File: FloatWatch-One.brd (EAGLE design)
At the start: 25.4 x 40 mm, 53 parts, among them Q1 S8050, Q2 S8050, U1 ATMEGA168P-QFN32, U2 ADXL345, U3 MCP6001-SOT23, U4 APDS-9008, U5 TP4055, U6 3.3V, U7 CH340E, Y1 7.3728MHz

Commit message: Rename to FloatWatch
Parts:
- removed POVLOGO: (no value), MyLibrary:ICON-PW
- added U$1: (no value), MyLibrary:ICON-OSHW
- moved CELOGO 2.01 mm to (19.7, 12.1)
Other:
- board text added: "Design by geneLocated"
- board text added: "Devised & Assembled in China"
- board text added: "FloatWatch"
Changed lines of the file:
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@@
 <board>
 <plain>
-<text x="8.8865" y="38.09" size="0.45" layer="22" font="vector" rot="MR180" align="bottom-right">Ver 1.1</text>
+<text x="19.685" y="34.925" size="0.8128" layer="22" font="vector" rot="MR0">Ver 1.1</text>
 <wire x1="1.27" y1="5.08" x2="0" y2="3.81" width="0" layer="20" curve="90"/>
 <wire x1="0" y1="3.81" x2="0" y2="1.27" width="0" layer="20"/>
@@
 <wire x1="1.27" y1="8.255" x2="24.13" y2="8.255" width="0" layer="20"/>
 <wire x1="24.13" y1="5.08" x2="1.27" y2="5.08" width="0" layer="20"/>
+<text x="19.685" y="36.195" size="1.778" layer="22" font="vector" rot="MR0">FloatWatch</text>
+<text x="19.685" y="10.795" size="0.762" layer="22" font="vector" rot="MR0">Design by geneLocated</text>
+<text x="19.685" y="10.16" size="0.5842" layer="22" font="vector" rot="MR0">Devised &amp; Assembled in China</text>
 </plain>
 <attributes>
@@
 </element>
 <element name="TS1" library="MyLibrary" package="TS-3X4P" value="TS-P" x="23.8125" y="24.13" rot="R90"/>
-<element name="CELOGO" library="MyLibrary" package="ICON-CE" value="" x="20.32" y="10.16" rot="MR0"/>
-<element name="POVLOGO" library="MyLibrary" package="ICON-PW" value="" x="18.7325" y="36.195" rot="MR0"/>
+<element name="CELOGO" library="MyLibrary" package="ICON-CE" value="" x="19.685" y="12.065" rot="MR0"/>
 <element name="U5" library="MyLibrary" package="SOT23-5" value="TP4055" x="6.985" y="35.8775" smashed="yes" rot="R180">
 <attribute name="VALUE" x="8.255" y="38.4175" size="0.6096" layer="27" font="vector" ratio="10" rot="R180" align="center-left"/>
@@
 <attribute name="VALUE" x="8.5725" y="26.67" size="0.6096" layer="27" font="vector" rot="R90"/>
 </element>
+<element name="U$1" library="MyLibrary" package="ICON-OSHW" value="" x="6.985" y="13.335" rot="MR0"/>
 </elements>
 <signals>

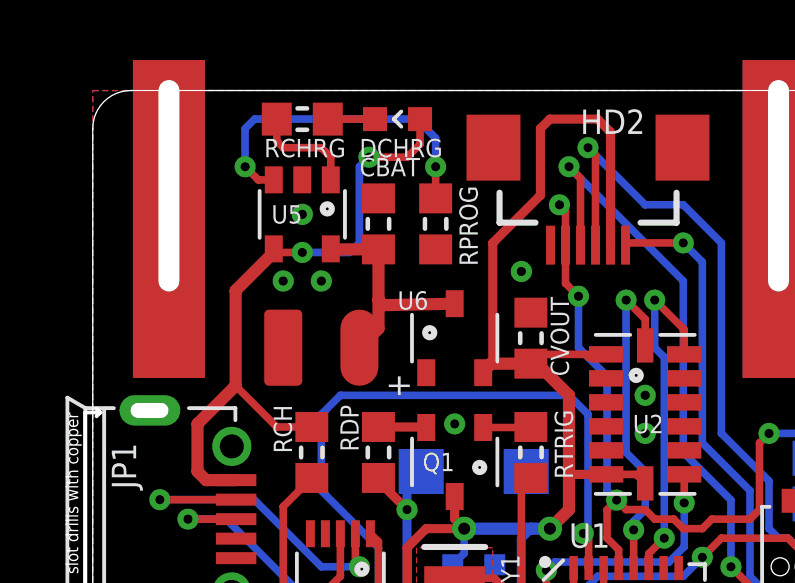
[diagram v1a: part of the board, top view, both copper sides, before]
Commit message: Fixes TP4055 footprint bug
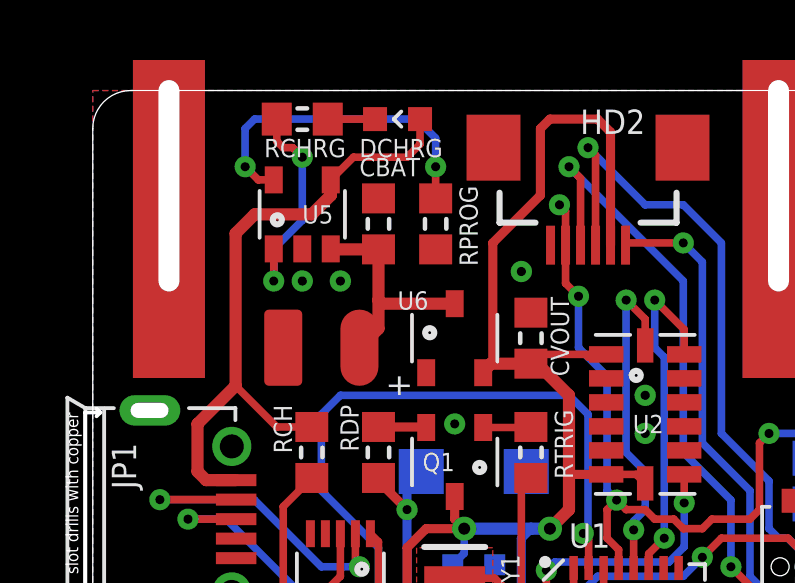
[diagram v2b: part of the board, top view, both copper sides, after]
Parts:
- turned U5 to 0 degrees
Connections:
- net PROG: now also U5.5; no longer U5.3
- net VBAT: now also U5.3; no longer U5.5
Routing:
- net !CHRG: track 3.51 -> 7.41 mm, vias 0 -> 2
- net VUSB: track 21.7 -> 21.5 mm, vias 2 -> 0
- net GND: vias 13 -> 12
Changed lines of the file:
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@@
 <?xml version="1.0" encoding="utf-8"?>
 <!DOCTYPE eagle SYSTEM "eagle.dtd">
-<eagle version="7.7.0">
+<eagle version="7.6.0">
 <drawing>
 <settings>
@@
 <setting verticaltext="up"/>
 </settings>
-<grid distance="25" unitdist="mil" unit="inch" style="lines" multiple="1" display="yes" altdistance="0.3175" altunitdist="mm" altunit="mm"/>
+<grid distance="25" unitdist="mil" unit="mm" style="lines" multiple="1" display="yes" altdistance="0.3175" altunitdist="mm" altunit="mm"/>
 <layers>
 <layer number="1" name="Top" color="4" fill="1" visible="yes" active="yes"/>
@@
 <element name="TS1" library="MyLibrary" package="TS-3X4P" value="TS-P" x="23.8125" y="24.13" rot="R90"/>
 <element name="CELOGO" library="MyLibrary" package="ICON-CE" value="" x="19.685" y="12.065" rot="MR0"/>
-<element name="U5" library="MyLibrary" package="SOT23-5" value="TP4055" x="6.985" y="35.8775" smashed="yes" rot="R180">
-<attribute name="VALUE" x="8.255" y="38.4175" size="0.6096" layer="27" font="vector" ratio="10" rot="R180" align="center-left"/>
-<attribute name="NAME" x="6.985" y="35.8775" size="0.6096" layer="25" font="vector" ratio="10" rot="R180" align="center-left"/>
+<element name="U5" library="MyLibrary" package="SOT23-5" value="TP4055" x="6.985" y="35.8775" smashed="yes">
+<attribute name="VALUE" x="5.715" y="33.3375" size="0.6096" layer="27" font="vector" ratio="10" align="center-left"/>
+<attribute name="NAME" x="6.985" y="35.8775" size="0.6096" layer="25" font="vector" ratio="10" align="center-left"/>
 </element>
 <element name="JP1" library="MyLibrary" package="USB-MICRO" value="USB-MICRO" x="1.905" y="25.7175" smashed="yes" rot="R270">
@@
 <contactref element="DP1" pad="C"/>
 <contactref element="LI-ION" pad="-"/>
-<via x="6.985" y="35.8775" extent="1-16" drill="0.3048"/>
 <contactref element="HD1" pad="5"/>
 <contactref element="HD1" pad="6"/>
@@
 <wire x1="16.125" y1="13.41" x2="16.125" y2="12.3825" width="0.3048" layer="1"/>
 <via x="13.97" y="11.43" extent="1-16" drill="0.3"/>
-<via x="6.35" y="33.655" extent="1-16" drill="0.3048"/>
-<via x="7.62" y="33.655" extent="1-16" drill="0.3048"/>
+<via x="6.985" y="33.655" extent="1-16" drill="0.3048"/>
+<via x="8.255" y="33.655" extent="1-16" drill="0.3048"/>
 <via x="18.415" y="28.575" extent="1-16" drill="0.3048"/>
 <via x="16.1925" y="22.225" extent="1-16" drill="0.3048"/>
@@
 <signal name="VBAT">
 <contactref element="U6" pad="3"/>
-<contactref element="U5" pad="5"/>
+<contactref element="U5" pad="3"/>
 <contactref element="CBAT" pad="1"/>
 <contactref element="LI-ION" pad="+"/>
-<wire x1="9.525" y1="34.71" x2="7.9525" y2="34.71" width="0.4064" layer="1"/>
-<wire x1="7.9525" y1="34.71" x2="7.935" y2="34.7275" width="0.4064" layer="1"/>
 <wire x1="9.525" y1="34.71" x2="9.525" y2="33.02" width="0.4064" layer="1"/>
 <wire x1="9.525" y1="33.02" x2="9.525" y2="32.0675" width="0.4064" layer="1"/>
 <wire x1="9.525" y1="32.0675" x2="8.89" y2="31.4325" width="0.4064" layer="1"/>
-<wire x1="12.065" y1="32.9" x2="9.695" y2="32.85" width="0.4064" layer="1"/>
-<wire x1="9.695" y1="32.85" x2="9.525" y2="33.02" width="0.4064" layer="1"/>
+<wire x1="9.525" y1="34.71" x2="7.9525" y2="34.71" width="0.4064" layer="1"/>
+<wire x1="7.9525" y1="34.71" x2="7.935" y2="34.7275" width="0.4064" layer="1"/>
+<wire x1="12.065" y1="32.9" x2="9.645" y2="32.9" width="0.4064" layer="1"/>
+<wire x1="9.645" y1="32.9" x2="9.525" y2="33.02" width="0.4064" layer="1"/>
 </signal>
 <signal name="RXD">
@@
 </signal>
 <signal name="PROG">
-<contactref element="U5" pad="3"/>
+<contactref element="U5" pad="5"/>
 <contactref element="RPROG" pad="1"/>
 <wire x1="11.43" y1="36.41" x2="11.43" y2="37.465" width="0.254" layer="1"/>
@@
 <wire x1="11.43" y1="38.4175" x2="10.795" y2="39.0525" width="0.254" layer="16"/>
 <wire x1="10.795" y1="39.0525" x2="5.3975" y2="39.0525" width="0.254" layer="16"/>
-<wire x1="6.0325" y1="37.025" x2="6.035" y2="37.0275" width="0.254" layer="1"/>
-<wire x1="6.0325" y1="37.025" x2="5.52" y2="37.025" width="0.254" layer="1"/>
-<wire x1="5.52" y1="37.025" x2="5.08" y2="37.465" width="0.254" layer="1"/>
 <via x="5.08" y="37.465" extent="1-16" drill="0.3"/>
 <wire x1="5.08" y1="37.465" x2="5.08" y2="38.735" width="0.254" layer="16"/>
 <wire x1="5.08" y1="38.735" x2="5.3975" y2="39.0525" width="0.254" layer="16"/>
+<wire x1="5.08" y1="37.465" x2="5.5175" y2="37.0275" width="0.254" layer="1"/>
+<wire x1="5.5175" y1="37.0275" x2="6.035" y2="37.0275" width="0.254" layer="1"/>
 </signal>
 <signal name="!CHRG">
 <contactref element="U5" pad="1"/>
 <contactref element="RCHRG" pad="1"/>
+<wire x1="6.035" y1="34.7275" x2="6.035" y2="33.655" width="0.254" layer="1"/>
+<wire x1="6.035" y1="33.655" x2="6.0325" y2="33.655" width="0.254" layer="1"/>
 <wire x1="6.135" y1="39.0525" x2="6.135" y2="38.315" width="0.254" layer="1"/>
 <wire x1="6.135" y1="38.315" x2="6.35" y2="38.1" width="0.254" layer="1"/>
-<wire x1="6.35" y1="38.1" x2="7.62" y2="38.1" width="0.254" layer="1"/>
-<wire x1="7.62" y1="38.1" x2="7.935" y2="37.785" width="0.254" layer="1"/>
-<wire x1="7.935" y1="37.785" x2="7.935" y2="37.0275" width="0.254" layer="1"/>
+<wire x1="6.35" y1="38.1" x2="6.6675" y2="38.1" width="0.254" layer="1"/>
+<wire x1="6.6675" y1="38.1" x2="6.985" y2="37.7825" width="0.254" layer="1"/>
+<via x="6.985" y="37.7825" extent="1-16" drill="0.3"/>
+<wire x1="6.985" y1="37.7825" x2="6.985" y2="35.6775" width="0.254" layer="16"/>
+<wire x1="6.985" y1="35.6775" x2="6.035" y2="34.7275" width="0.254" layer="16"/>
+<wire x1="6.035" y1="34.7275" x2="6.035" y2="33.6575" width="0.254" layer="16"/>
+<wire x1="6.035" y1="33.6575" x2="6.0325" y2="33.655" width="0.254" layer="16"/>
+<via x="6.0325" y="33.655" extent="1-16" drill="0.3"/>
 </signal>
 <signal name="DRCHRG">
@@
 <wire x1="10.91" y1="39.0525" x2="10.91" y2="38.215" width="0.254" layer="1"/>
 <wire x1="10.91" y1="38.215" x2="10.4775" y2="37.7825" width="0.254" layer="1"/>
-<wire x1="9.2075" y1="37.7825" x2="8.89" y2="37.465" width="0.254" layer="16"/>
-<wire x1="8.89" y1="37.465" x2="8.89" y2="34.925" width="0.254" layer="16"/>
-<wire x1="8.89" y1="34.925" x2="8.5725" y2="34.6075" width="0.254" layer="16"/>
-<wire x1="8.5725" y1="34.6075" x2="6.985" y2="34.6075" width="0.254" layer="16"/>
-<via x="6.985" y="34.6075" extent="1-16" drill="0.3"/>
-<wire x1="6.985" y1="34.6075" x2="6.155" y2="34.6075" width="0.254" layer="1"/>
-<wire x1="6.155" y1="34.6075" x2="6.035" y2="34.7275" width="0.254" layer="1"/>
-<wire x1="10.4775" y1="37.7825" x2="9.2075" y2="37.7825" width="0.254" layer="1"/>
-<via x="9.2075" y="37.7825" extent="1-16" drill="0.3"/>
-<wire x1="4.7625" y1="33.3375" x2="6.035" y2="34.61" width="0.4064" layer="1"/>
-<wire x1="6.035" y1="34.61" x2="6.035" y2="34.7275" width="0.4064" layer="1"/>
-<wire x1="4.7625" y1="33.3375" x2="4.7625" y2="30.1625" width="0.4064" layer="1"/>
+<wire x1="10.4775" y1="37.7825" x2="8.69" y2="37.7825" width="0.254" layer="1"/>
+<wire x1="4.7625" y1="35.2425" x2="4.7625" y2="30.1625" width="0.4064" layer="1"/>
 <contactref element="RCH" pad="2"/>
 <wire x1="4.7625" y1="30.1625" x2="3.4925" y2="28.8925" width="0.4064" layer="1"/>
@@
 <wire x1="7.3025" y1="28.79" x2="6.135" y2="28.79" width="0.254" layer="1"/>
 <wire x1="6.135" y1="28.79" x2="4.7625" y2="30.1625" width="0.254" layer="1"/>
+<wire x1="4.7625" y1="35.2425" x2="5.3975" y2="35.8775" width="0.4064" layer="1"/>
+<wire x1="5.3975" y1="35.8775" x2="7.3025" y2="35.8775" width="0.4064" layer="1"/>
+<wire x1="7.3025" y1="35.8775" x2="7.935" y2="36.51" width="0.4064" layer="1"/>
+<wire x1="7.935" y1="36.51" x2="7.935" y2="37.0275" width="0.4064" layer="1"/>
+<wire x1="8.69" y1="37.7825" x2="7.935" y2="37.0275" width="0.254" layer="1"/>
 </signal>
 <signal name="UD-">

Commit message: Fixes RPROG resistance
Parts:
- RPROG: value 1kΩ -> 1.66kΩ+
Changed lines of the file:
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@@
 <?xml version="1.0" encoding="utf-8"?>
 <!DOCTYPE eagle SYSTEM "eagle.dtd">
-<eagle version="7.6.0">
+<eagle version="7.7.0">
 <drawing>
 <settings>
@@
 <attribute name="VALUE" x="10.795" y="26.67" size="0.6096" layer="27" font="vector" rot="R90"/>
 </element>
-<element name="RPROG" library="MyLibrary" package="SMD0603" value="1kΩ" x="11.43" y="35.56" smashed="yes" rot="R270">
+<element name="RPROG" library="MyLibrary" package="SMD0603" value="1.66kΩ+" x="11.43" y="35.56" smashed="yes" rot="R270">
 <attribute name="NAME" x="12.22375" y="36.83" size="0.6096" layer="25" font="vector" rot="R270"/>
 <attribute name="VALUE" x="10.16" y="36.83" size="0.6096" layer="27" font="vector" rot="R270"/>
